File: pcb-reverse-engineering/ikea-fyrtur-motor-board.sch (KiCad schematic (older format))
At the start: 43 parts, among them IC1 HT75xx-1-SOT89, IC10 LM321, IC2 BC847BS, IC3 IRF5851, IC4 IRF5851, IC5 STM32F030K6Tx, IC7 BC847BPN ?, IC8 SS360S, IC9 SS360S, J4 MOTOR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

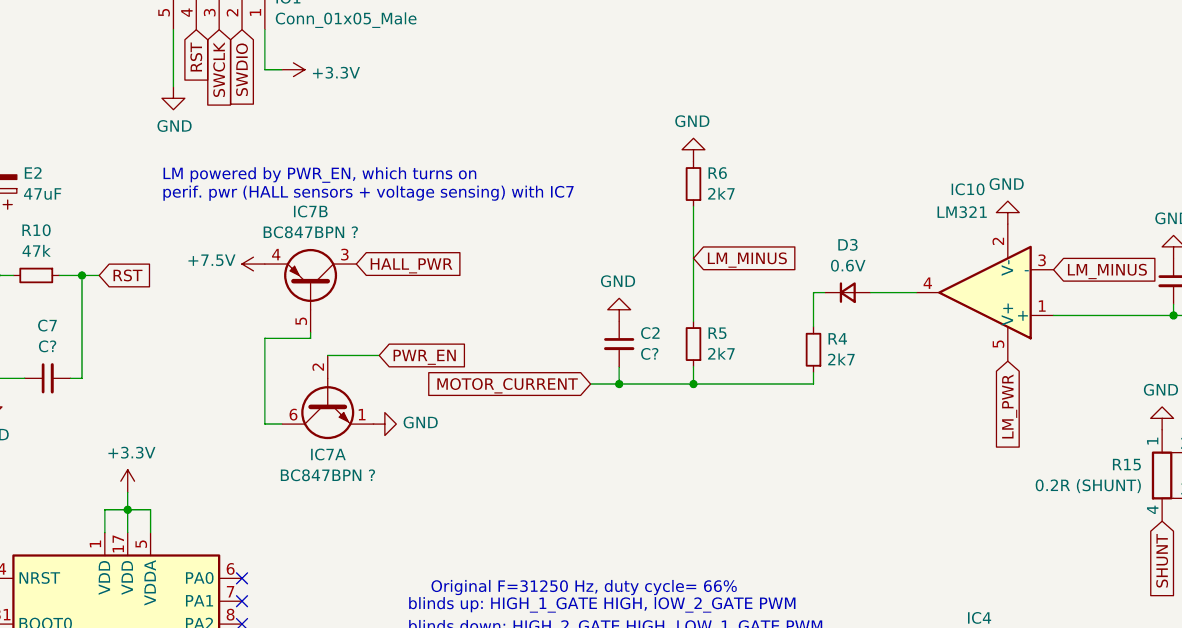
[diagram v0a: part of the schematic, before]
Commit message: Fixed LM_PWR to PWR_EN
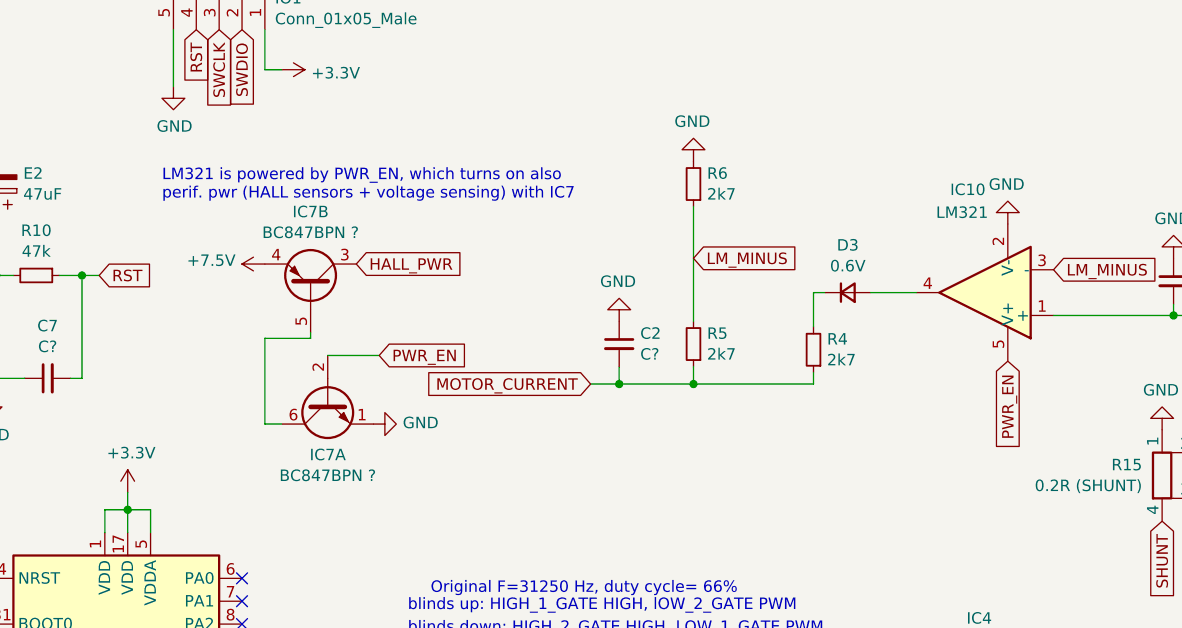
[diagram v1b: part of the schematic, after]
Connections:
- net LM_PWR is gone; now on net PWR_EN: IC10.5 (V+)
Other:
- note added: "LM321 is powered by PWR_EN, which turns on also \nperif. pwr (HALL sensors + voltage sensing) with IC7"
- note removed: "LM powered by PWR_EN, which turns on \nperif. pwr (HALL sensors + voltage sensing) with IC7"
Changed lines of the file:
@@
 $EndComp
 Text GLabel 7825 2550 3    50   Input ~ 0
-LM_PWR
+PWR_EN
 Text GLabel 5075 2525 2    50   Input ~ 0
 PWR_EN
@@
 NoConn ~ 1450 3950
 Text Notes 4125 1850 0    50   ~ 0
-LM powered by PWR_EN, which turns on \nperif. pwr (HALL sensors + voltage sensing) with IC7
+LM321 is powered by PWR_EN, which turns on also \nperif. pwr (HALL sensors + voltage sensing) with IC7
 Text Notes 5250 4525 0    50   ~ 0
 High side mosfets turned on \nby double NPN transistor. \nLow side mosfets controlled \ndirectly by STM32
